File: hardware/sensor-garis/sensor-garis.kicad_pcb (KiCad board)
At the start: 2 copper layers, 120 x 52 mm, 41 parts, among them J1 Conn_01x08_Socket, U1 QRE1113GR, U10 QRE1113GR, U11 QRE1113GR, U12 QRE1113GR, U13 CD74HC4067M, U2 QRE1113GR, U3 QRE1113GR, U4 QRE1113GR, U5 QRE1113GR, U6 QRE1113GR, U7 QRE1113GR, U8 QRE1113GR, U9 QRE1113GR

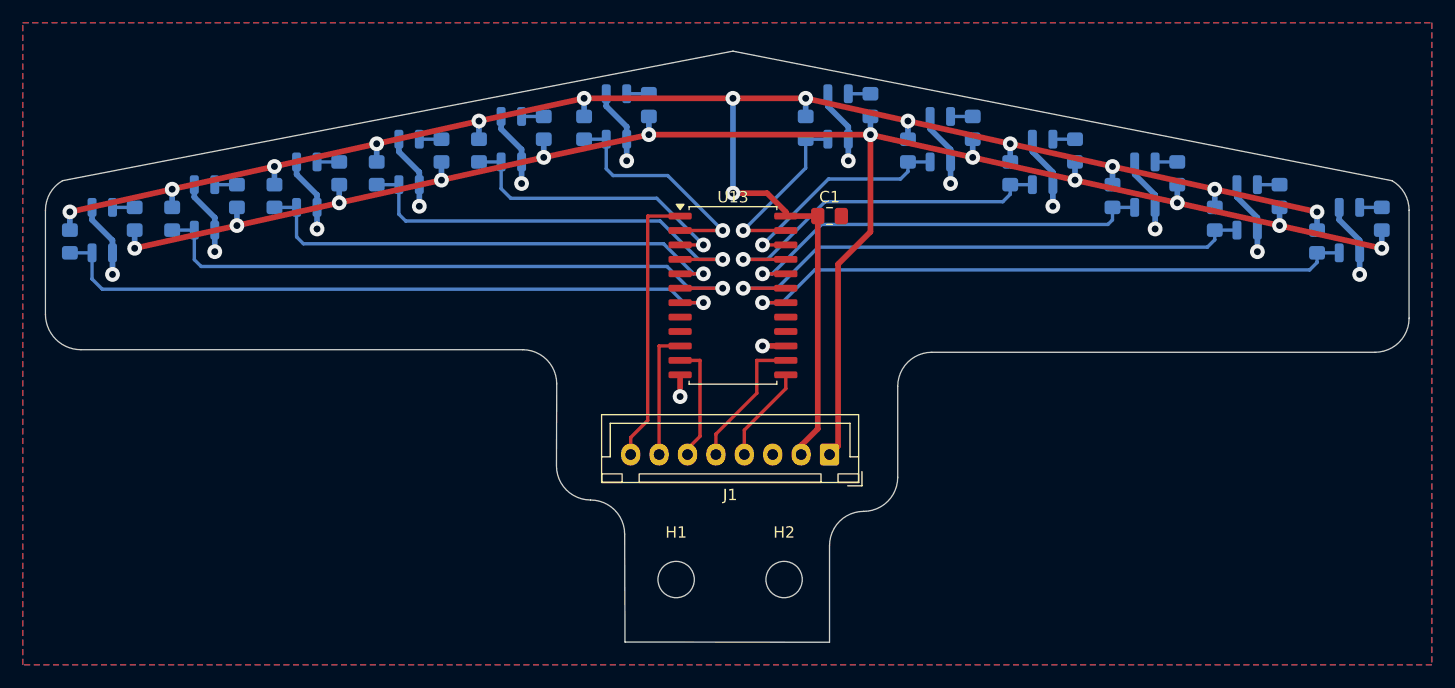
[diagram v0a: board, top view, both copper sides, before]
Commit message: PCB sensor rev B: bentuk jangkar, 12 QRE jarak 8 mm di busur
Sensor tengah hampir lurus, lengan melengkung ke belakang (5/5/12/25/40 derajat),
pita + kait + tangkai, lebar 95 mm. Routing ulang (S di B, daya di F, pour GND
2 sisi), DRC 0 error / 0 unconnected. Salinan + gambar di revisi/rev-b/, catatan
dan koordinat sensor untuk firmware di REVISI.md, skrip penataan di
hardware/tools/sensor_revb_layout.py.

Co-Authored-By: Claude Opus 5.5 <noreply@anthropic.com>
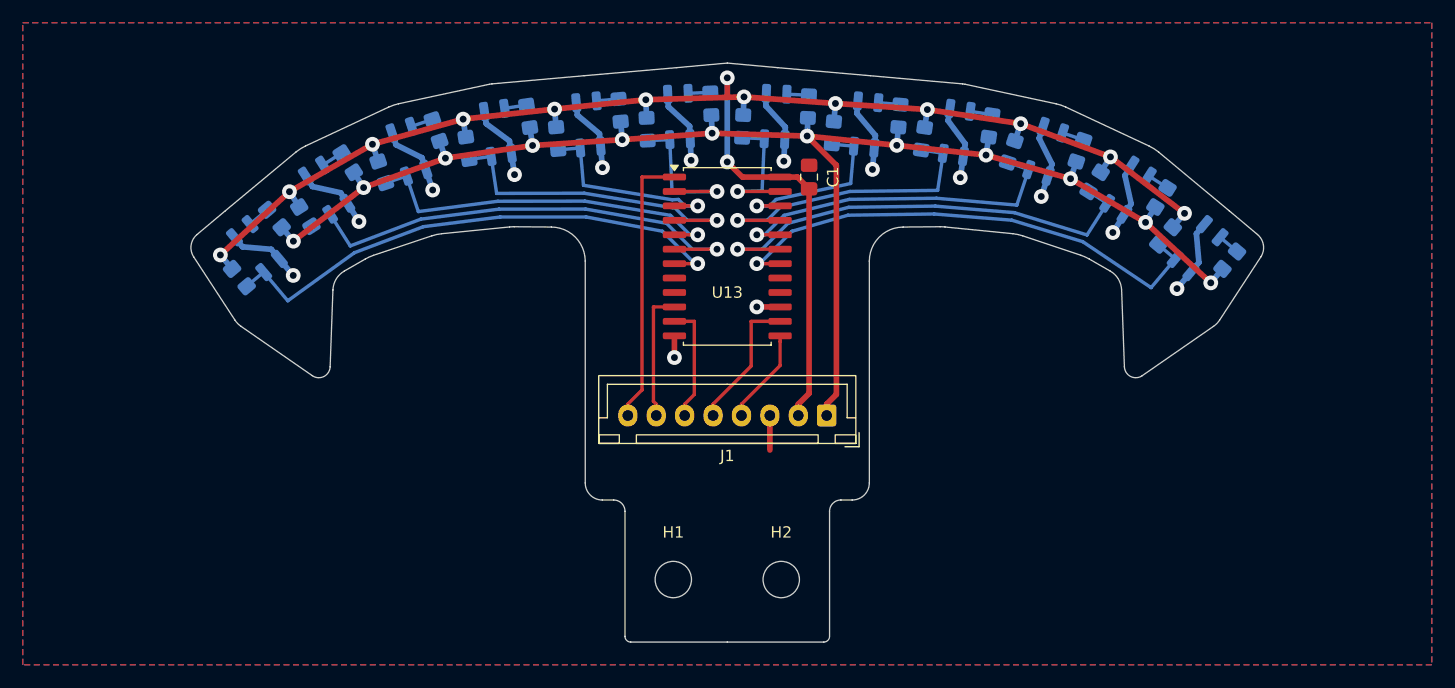
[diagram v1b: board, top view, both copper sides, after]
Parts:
- moved R2 15.3 mm to (157.1, 68.4), turned to 130 degrees
- moved R23 13.9 mm to (244.2, 66.9), turned to 50 degrees
- moved U1 13.7 mm to (158.6, 65.8), turned to -140 degrees
- moved U12 13.5 mm to (241.4, 65.8), turned to 140 degrees
- moved R24 13.3 mm to (238.6, 64.8), turned to 50 degrees
- moved R1 12.3 mm to (160.1, 63.2), turned to 130 degrees
- moved R4 11.7 mm to (162.9, 63.1), turned to 122.5 degrees
- moved R22 11.1 mm to (232.3, 60.0), turned to 57.5 degrees
- moved U2 10.8 mm to (164.7, 60.7), turned to -147.5 degrees
- moved U11 10.6 mm to (235.3, 60.7), turned to 147.5 degrees
- moved R21 10.4 mm to (238.2, 61.4), turned to 57.5 degrees
- moved R3 10.2 mm to (166.6, 58.3), turned to 122.5 degrees
- moved R20 9.72 mm to (225.0, 57.4), turned to 71.5 degrees
- moved R6 9.68 mm to (169.6, 59.2), turned to 108.5 degrees
- moved U3 9.46 mm to (172.0, 57.3), turned to -161.5 degrees
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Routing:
- net +5V: track 160.8 -> 131.6 mm
- net +3V3: track 169.6 -> 147.7 mm
- net S1: track 61.0 -> 46.5 mm
- net S2: track 55.8 -> 42.8 mm
- net S3: track 43.7 -> 32.8 mm
- net S12: track 55.1 -> 44.9 mm
- net S4: track 38.4 -> 29.0 mm
- net S11: track 49.8 -> 41.2 mm
- net S5: track 26.2 -> 17.7 mm
- net S10: track 37.9 -> 31.1 mm
- net S6: track 20.8 -> 14.3 mm
- net S9: track 32.4 -> 27.2 mm
- net S8: track 20.3 -> 15.9 mm
- net S7: track 16.0 -> 12.5 mm
- net GND: track 83.7 -> 86.7 mm
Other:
- board size 120 x 52 mm -> 94.4 x 51 mm
